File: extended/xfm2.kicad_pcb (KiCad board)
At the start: 2 copper layers, 181.4 x 70.6 mm, 85 parts, among them IC1 74LVC1G07QSE-7, IC2 74LVC1G07QSE-7, J1 Midi In, J10 10137062-00021LF, J2 Pin Breakout, J3 Midi Out, J4 Midi Thru, J5 Conn_Coaxial, J6 Jack-DC, J7 A-100_Bus_Connector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

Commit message: Next bugfix version 1.33.
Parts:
- C14, C15, C9: value 0.1uF -> 100nF
- C8: value 0.33uF -> 330nF
- IC1, IC2: footprint samacsys:SOT65P210X110-5N -> Package_TO_SOT_SMD:SOT-353_SC-70-5_Handsoldering
- J10: value 10137062-00021LF -> USB4105-GF-A; footprint samacsys:CONN_10137062-00021LF -> GCT_USB4105-GF-A
- REF** (x4): value MountingHole_2.7mm_M2.5_ISO7380 -> MountingHole_2.7mm_M2.5_ISO7380_Pad; footprint MountingHole:MountingHole_2.7mm_M2.5_ISO7380 -> MountingHole:MountingHole_2.7mm_M2.5_ISO7380_Pad
- moved R25 13.5 mm to (183.4, 150.9), turned to 90 degrees
- moved C18 13.2 mm to (205.5, 105.2)
- moved R21 11.7 mm to (205.5, 101.7)
- moved IC2 7.63 mm to (205.7, 98.0)
- moved J10 4.45 mm to (193.3, 151.8)
- moved IC1 4.14 mm to (175.3, 88.4), turned to 90 degrees
- moved R20 3.81 mm to (177.8, 87.9), turned to 90 degrees
- moved R22 3.20 mm to (172.7, 87.9)
- moved C17 3.07 mm to (170.7, 87.9)
- moved R23 2.55 mm to (211.1, 96.6)
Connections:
- IC1 pad 2: UART_RX_5V -> UART_TX_5V
- IC2 pad 4: UART_TX_5V -> UART_RX_5V
- J10 pad B6: Net-(J10-PadB6) -> /D+
- J10 pad B7: Net-(J10-PadB7) -> /D-
- J10 pad S1: (no net) -> GND
- J10 pad S2: (no net) -> GND
- J10 pad S3: (no net) -> GND
- J10 pad S4: (no net) -> GND
- R21 pad 1: UART_TX_5V -> UART_RX_5V
- R22 pad 2: UART_RX_5V -> UART_TX_5V
- R24 pad 2: Net-(J10-PadA5) -> Net-(J10-PadB5)
- R25 pad 2: Net-(J10-PadB5) -> Net-(J10-PadA5)
- U10 pad 1: UART_RX_5V -> UART_TX_5V
- U10 pad 5: UART_TX_5V -> UART_RX_5V
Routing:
- net +5V: track 208.3 -> 186.5 mm, vias 4 -> 7
- net UART_RX_3.3V_FPGA: track 59.9 -> 44.4 mm
- net GND: track 101.5 -> 86.7 mm, vias 8 -> 7
- net /D-: track 15.6 -> 24.0 mm, vias 0 -> 2
- net /VBUS: track 42.3 -> 47.7 mm, vias 4 -> 6
- net UART_RX_5V: track 66.0 -> 61.0 mm
- net Net-(J10-PadB5): track 15.3 -> 10.6 mm
- net UART_TX_5V: track 60.5 -> 64.4 mm
- net Net-(J10-PadA5): track 7.10 -> 10.3 mm
- net -5V: track 256.6 -> 259.8 mm
- net /D+: track 15.7 -> 18.7 mm
- net UART_TX_3.3V_FPGA: track 76.3 -> 78.5 mm
- net SPDIF_OUT: track 204.0 -> 204.6 mm, vias 5 -> 6
- net I2S_MUTE: track 127.8 -> 128.1 mm, vias 1 -> 3
- net +3V3: track 408.8 -> 408.9 mm, vias 14 -> 16
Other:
- rule trace_min: 0.2 -> 0.127
- board text added: "K"
- board text added: "Red Strp"
- board text added: "xfm2/xva1 extended board v1.33"
- board text removed: "Red Stripe"
- board text removed: "xfm2/xva1 extended board v1.3"

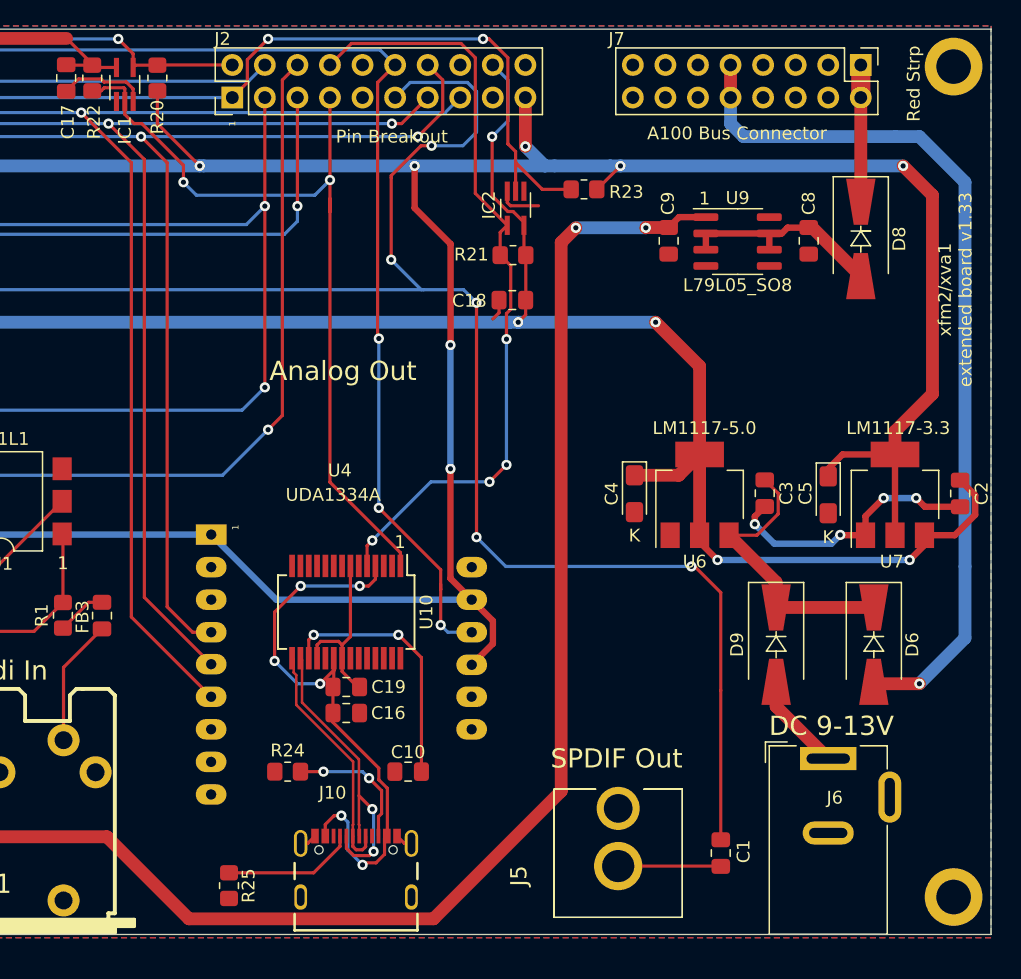
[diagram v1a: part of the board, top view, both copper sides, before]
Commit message: bugfix incl. gerber v1.34 for the extended board.
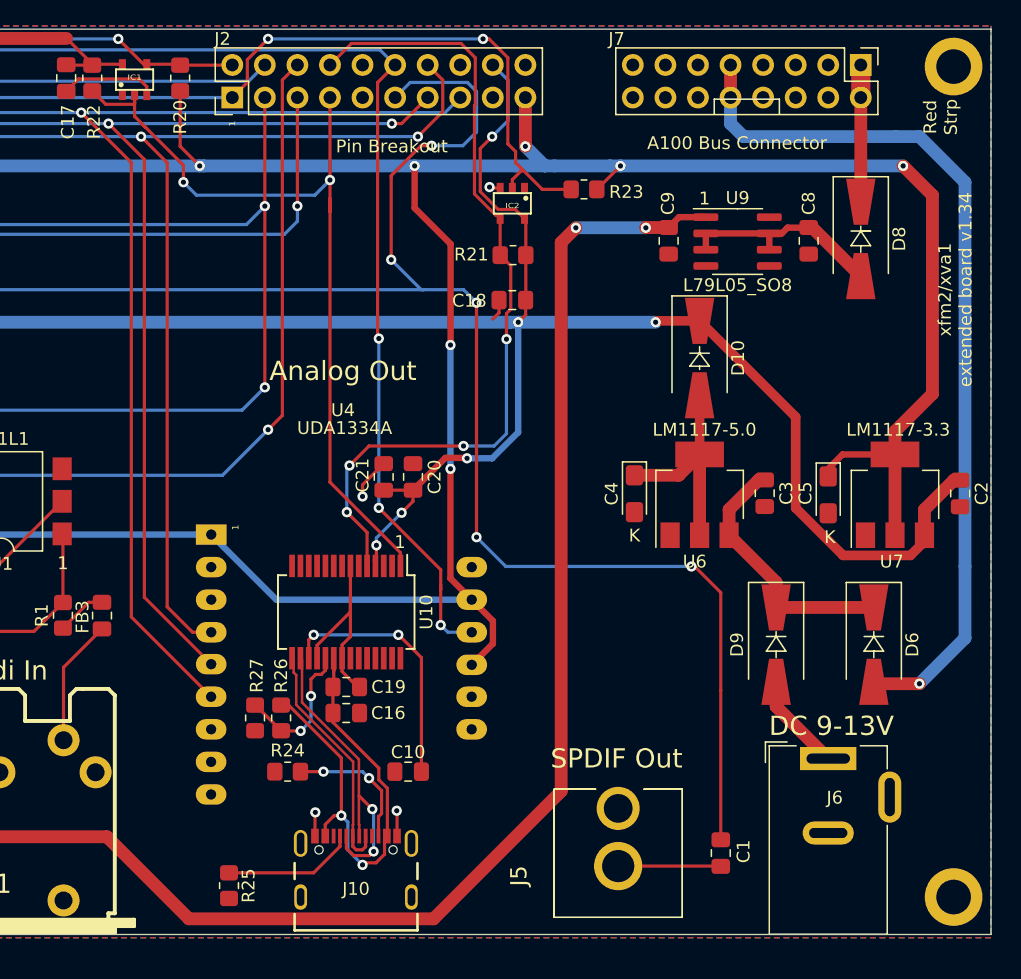
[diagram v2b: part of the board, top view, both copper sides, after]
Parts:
- added C20: 10nF, Capacitor_SMD:C_0805_2012Metric_Pad1.18x1.45mm_HandSolder, F.Cu at (197.7, 119.0)
- added C21: 0.1uF, Capacitor_SMD:C_0805_2012Metric_Pad1.18x1.45mm_HandSolder, F.Cu at (195.5, 119.0)
- added D10: 1N5819/SS14, Diode_SMD:D_SMA-SMB_Universal_Handsoldering, F.Cu at (220.1, 109.7)
- added R26: 4.7k, Resistor_SMD:R_0805_2012Metric_Pad1.20x1.40mm_HandSolder, F.Cu at (187.5, 137.8)
- added R27: 10k, Resistor_SMD:R_0805_2012Metric_Pad1.20x1.40mm_HandSolder, F.Cu at (185.4, 137.8)
- IC1, IC2: footprint Package_TO_SOT_SMD:SOT-353_SC-70-5_Handsoldering -> greatscott:SOT25
- J10: footprint GCT_USB4105-GF-A -> samacsys:GCT_USB4105-GF-A
- moved R20 1.78 mm to (179.6, 87.9)
- moved IC1 0.85 mm to (176.0, 88.0), turned to 0 degrees
- moved IC2 0.46 mm to (205.5, 97.7), turned to 180 degrees
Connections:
- C4 pad 1: +5V -> Net-(C4-Pad1)
- J10 pad S1: GND -> Net-(J10-PadS1)
- J10 pad S2: GND -> Net-(J10-PadS2)
- J10 pad S3: GND -> Net-(J10-PadS3)
- J10 pad S4: GND -> Net-(J10-PadS4)
- U10 pad 4: /VBUS -> +5V
- U6 pad 2: +5V -> Net-(C4-Pad1)
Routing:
- net +5V: track 186.5 -> 205.1 mm, vias 7 -> 8
- net Net-(C4-Pad1): track 0.00 -> 17.2 mm
- net GND: track 86.7 -> 70.4 mm
- net Net-(R26-Pad2): track 0.00 -> 11.1 mm, vias 0 -> 2
- net /VBUS: track 47.7 -> 39.1 mm, vias 6 -> 2
- net UART_RX_5V: track 61.0 -> 65.1 mm
- net Net-(C3-Pad1): track 22.6 -> 20.7 mm
- net UART_TX_5V: track 64.4 -> 65.4 mm
- net UART_RX_3.3V_FPGA: track 44.4 -> 43.6 mm
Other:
- net class 12v: clearance 0.2 -> 0.199
- net class Default: clearance 0.2 -> 0.199
- net class power 3-5v: clearance 0.2 -> 0.19
- rule trace_clearance: 0.2 -> 0.199
- rule trace_min: 0.127 -> 0
- board text added: "xfm2/xva1 extended board v1.34"
- board text removed: "xfm2/xva1 extended board v1.33"

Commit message: version 1.40 with kicad 6 migration
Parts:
- moved R20 10.4 mm to (169.2, 87.9)
- moved C17 10.4 mm to (160.3, 87.9)
- moved IC1 10.4 mm to (165.6, 88.0)
- moved R22 10.4 mm to (162.3, 87.9)
- moved J2 5.33 mm to (178.3, 89.4)
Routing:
- net SPDIF_OUT: track 204.6 -> 191.4 mm, vias 6 -> 5
- net +5V: track 205.1 -> 194.2 mm, vias 8 -> 7
- net MIDI_IN: track 174.8 -> 164.6 mm
- net GND: track 70.4 -> 61.1 mm
- net UART_RX_3.3V_FPGA: track 43.6 -> 36.3 mm, vias 2 -> 1
- net MIDI_OUT: track 164.6 -> 158.2 mm, vias 7 -> 6
- net MIDI_IN_INV: track 159.9 -> 154.1 mm
- net I2S_SCK: track 118.8 -> 113.1 mm, vias 1 -> 2
- net I2S_WS: track 119.8 -> 115.1 mm
- net I2S_MUTE: track 128.1 -> 123.5 mm
- net I2S_SDA: track 115.2 -> 110.8 mm
- net UART_TX_3.3V_FPGA: track 78.1 -> 82.5 mm, vias 2 -> 4
- net UART_TX_5V: track 65.4 -> 69.7 mm, vias 2 -> 3
- net UART_RX_5V: track 65.1 -> 67.8 mm, vias 4 -> 6
- net /VBUS: track 39.1 -> 37.1 mm
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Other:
- net class 12v removed
- net class Default removed
- net class power 3-5v removed
- board text added: "xfm2/xva1 extended board v1.4"
- board text removed: "xfm2/xva1 extended board v1.34"
